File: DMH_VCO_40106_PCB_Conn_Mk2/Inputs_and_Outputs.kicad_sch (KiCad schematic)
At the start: 11 parts, among them J1 TS_Jack_6.35mm_Sw, J150 Conn_01x12, J2 TS_Jack_6.35mm_Sw, J200 IDC_02x05, J3 TS_Jack_6.35mm_Sw, J4 TS_Jack_6.35mm_Sw, J5 TS_Jack_6.35mm_Sw, J6 TS_Jack_6.35mm_Sw, J7 TS_Jack_6.35mm_Sw, J8 TS_Jack_6.35mm_Sw, J9 TS_Jack_6.35mm_Sw

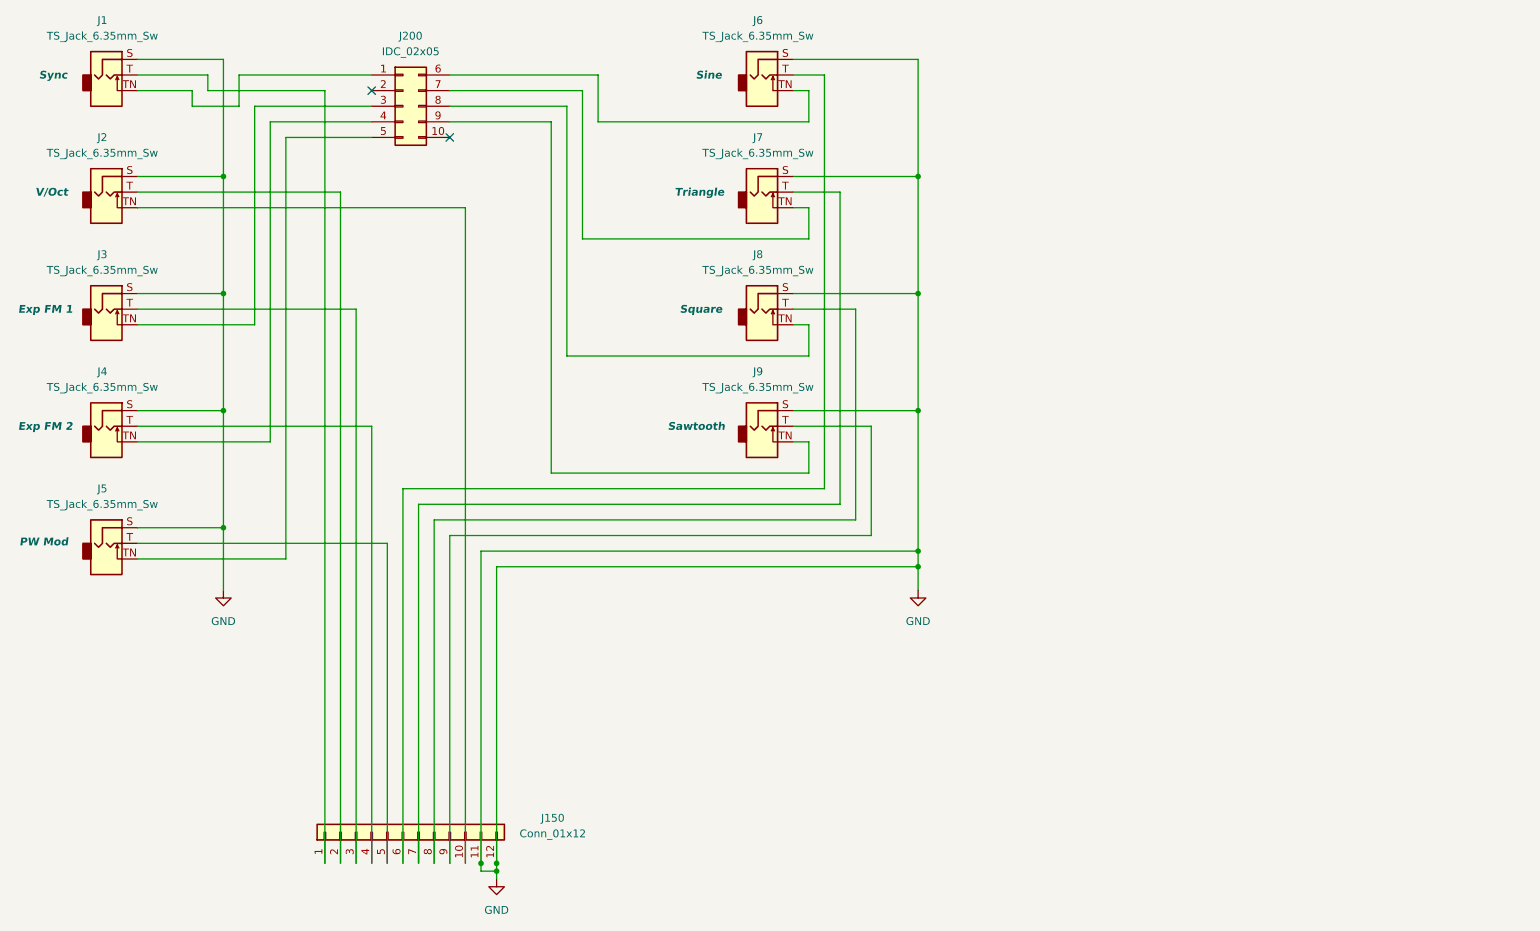
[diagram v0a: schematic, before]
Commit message: Routed Mk2 conn PCB
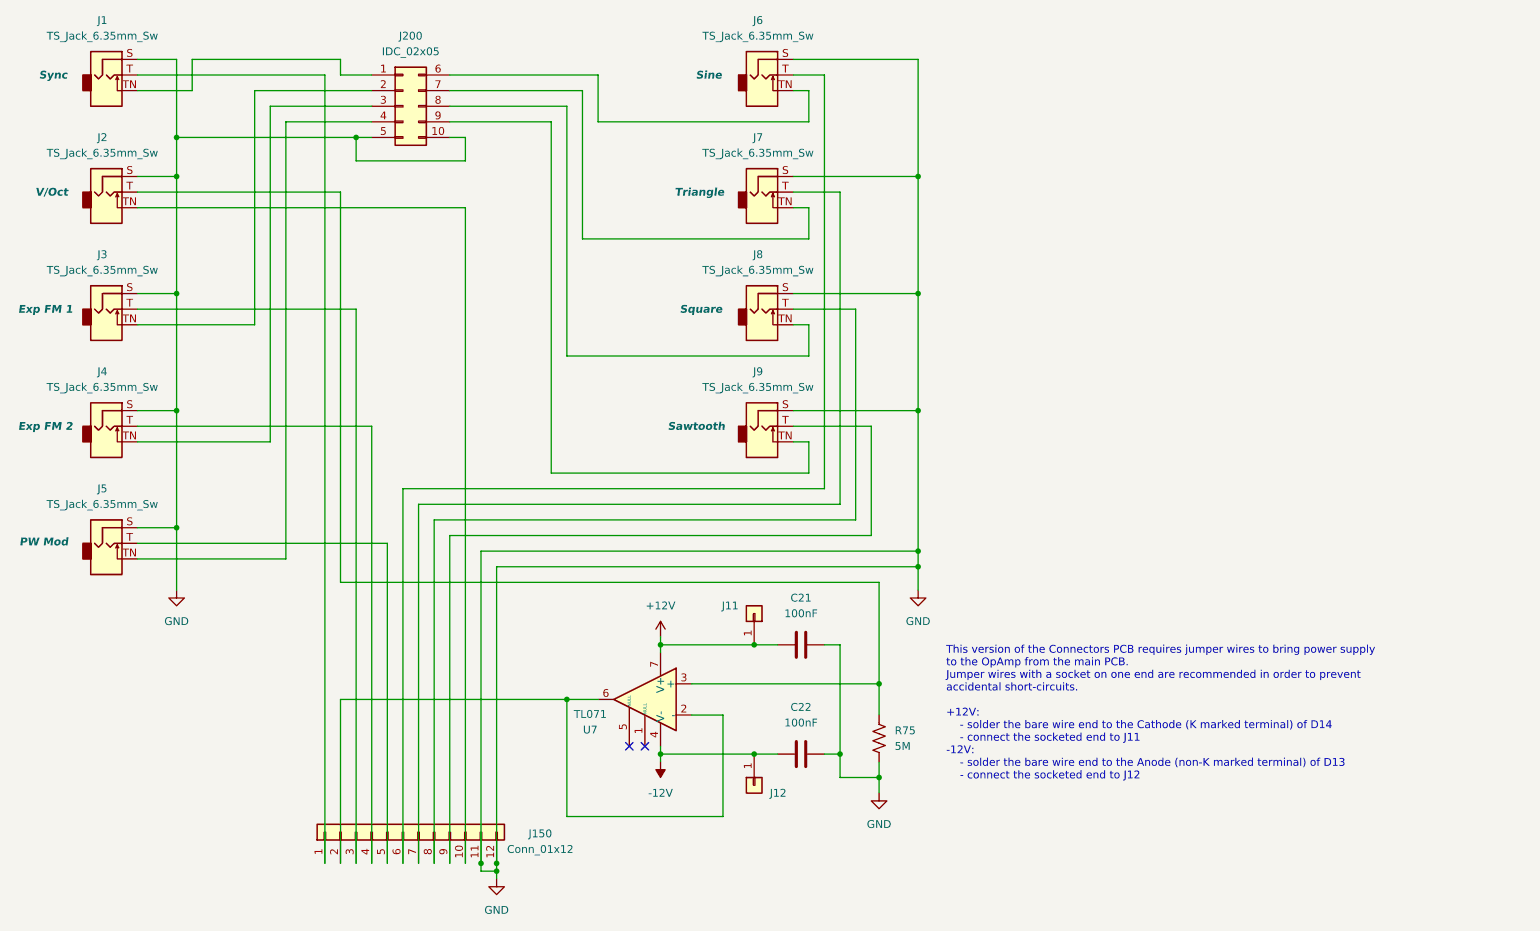
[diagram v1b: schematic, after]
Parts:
- added C21, C22: 100nF, Capacitor_THT:C_Disc_D4.3mm_W1.9mm_P5.00mm, symbol Device:C
- added J11, J12: Conn_01x01, Connector_PinHeader_2.54mm:PinHeader_1x01_P2.54mm_Vertical, symbol Connector_Generic:Conn_01x01
- added R75: 5M, Resistor_THT:R_Axial_DIN0207_L6.3mm_D2.5mm_P7.62mm_Horizontal, symbol Device:R_US
- added U7: TL071, Package_DIP:DIP-8_W7.62mm_Socket, symbol Amplifier_Operational:TL071
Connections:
- net GND: now also J200.10 (Pin_10), J200.5 (Pin_5), C21.2, C22.2, R75.1
- net at J3.TN: now also J200.2 (Pin_2); no longer J200.3 (Pin_3)
- net at J2.T: now also R75.2, U7.3 (+); no longer J150.2 (Pin_2)
- net at J4.TN: now also J200.3 (Pin_3); no longer J200.4 (Pin_4)
- net at J5.TN: now also J200.4 (Pin_4); no longer J200.5 (Pin_5)
- new net: J150.2 (Pin_2), U7.2 (-), U7.6
- new net +12V: C21.1, J11.1 (Pin_1), U7.7 (V+)
- new net -12V: C22.1, J12.1 (Pin_1), U7.4 (V-)
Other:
- note added: "This version of the Connectors PCB requires jumper wires to bring power supply to the OpAmp from the main PCB. Jumper wires with a socket on one end are recommended in order to prevent accidental short-circuits. +12V: - solder the bare wire end to the Cathode (K marked terminal) of D14 - connect the socketed end to J11 -12V: - solder the bare wire end to the Anode (non-K marked terminal) of D13 -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"

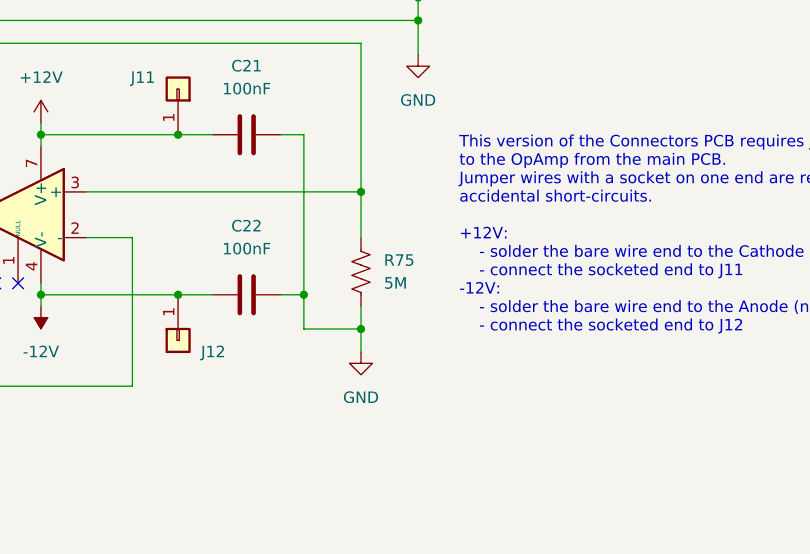
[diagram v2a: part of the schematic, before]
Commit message: Changed buffer resistor to 10M
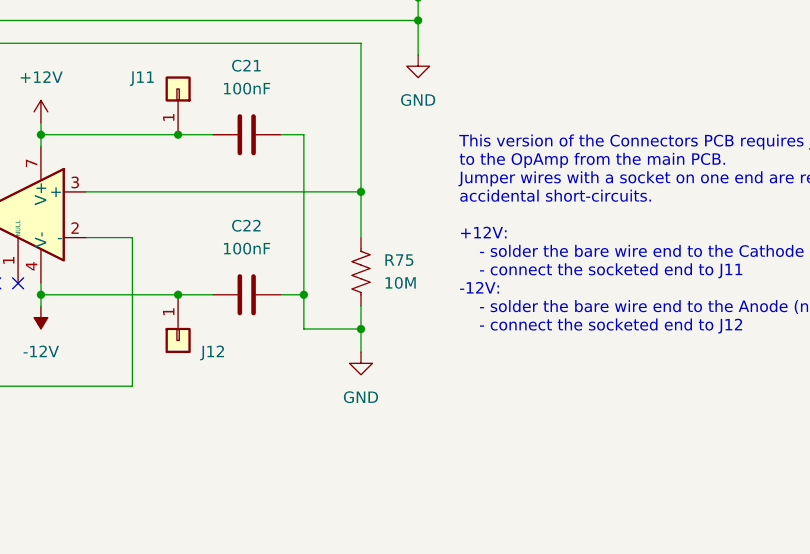
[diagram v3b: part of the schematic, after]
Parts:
- R75: value 5M -> 10M
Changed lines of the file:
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@@
 			)
 		)
-		(property "Value" "5M"
+		(property "Value" "10M"
 			(at 193.04 134.6199 0)
 			(effects
